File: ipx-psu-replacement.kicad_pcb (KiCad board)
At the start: 2 copper layers, 226 x 81 mm, 16 parts, among them J1 L, J10 -12V, J11 GND, J2 AC IN, J3 GND, J4 Floppy, J5 AC OUT, J6 N, J7 +12V, J8 +5V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

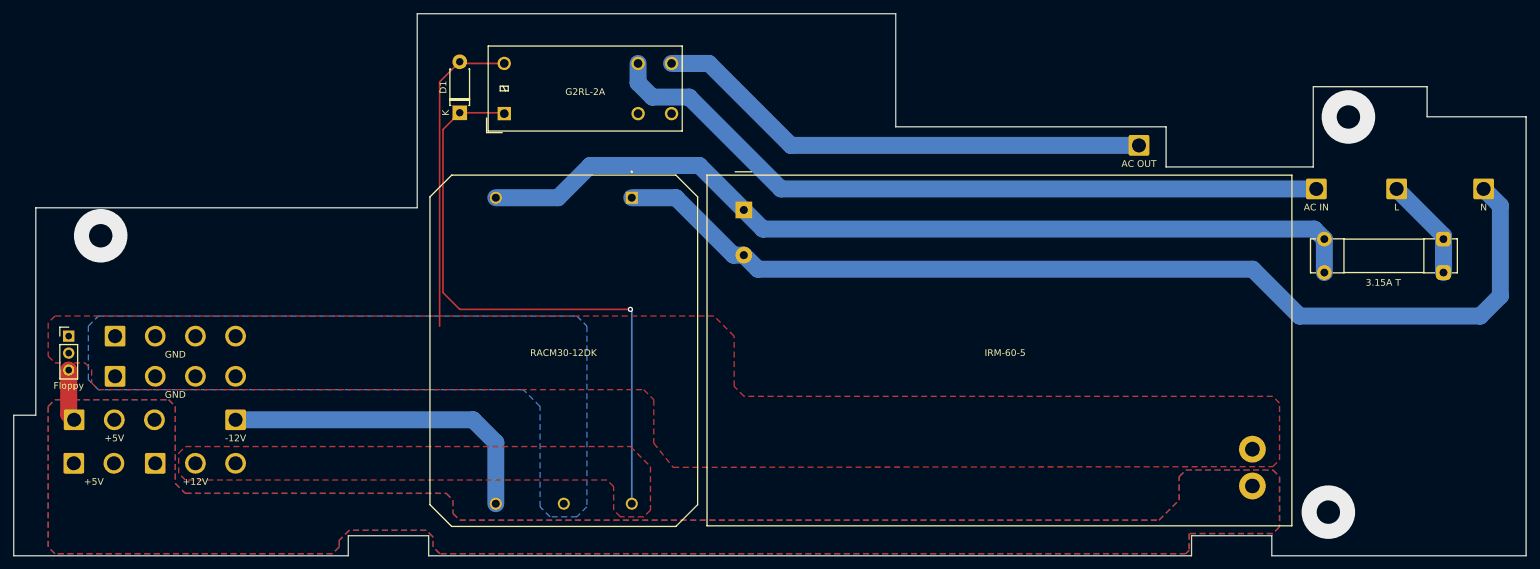
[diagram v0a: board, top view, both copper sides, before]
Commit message: add power good sensing
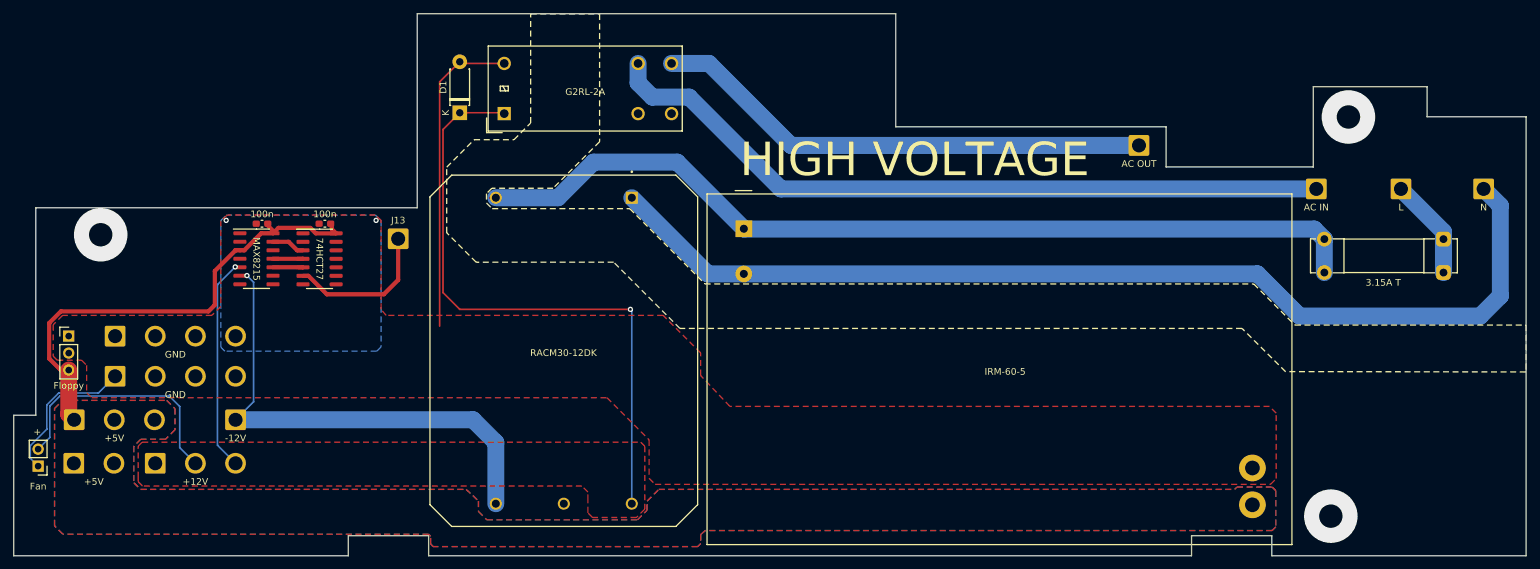
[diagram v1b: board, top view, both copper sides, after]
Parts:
- added C1: 100n, Capacitor_SMD:C_0603_1608Metric_Pad1.08x0.95mm_HandSolder, F.Cu at (76.5, 90.2)
- added C2: 100n, Capacitor_SMD:C_0603_1608Metric_Pad1.08x0.95mm_HandSolder, F.Cu at (85.8, 90.2)
- added J12: Fan, Connector_PinHeader_2.54mm:PinHeader_1x02_P2.54mm_Vertical, F.Cu at (43.0, 126.4)
- added J13: SENS, Connector_Wire:SolderWire-1.5sqmm_1x01_D1.7mm_OD3mm, F.Cu at (96.8, 92.5)
- added U1: 74HCT27, Package_SO:SO-14_3.9x8.65mm_P1.27mm, F.Cu at (85.0, 95.5)
- added U2: MAX8215, Package_SO:SO-14_3.9x8.65mm_P1.27mm, F.Cu at (75.6, 95.4)
- moved PS1 2.81 mm to (148.4, 91.0)
- moved J1 0.65 mm to (246.7, 85.0)
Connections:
- net /GND renamed GND
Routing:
- net /+12V: track 92.8 -> 162.4 mm, vias 1 -> 2
- net /+5V: track 7.77 -> 72.1 mm
- net /-12V: track 49.4 -> 73.6 mm, vias 0 -> 1
- net GND: track 47.5 -> 70.1 mm, vias 0 -> 2
- net Net-(J13-Pin_1): track 0.00 -> 22.4 mm
- net Net-(U2-OUT1): track 0.00 -> 5.01 mm
- net Net-(U2-OUT4): track 0.00 -> 4.48 mm
- net Net-(U2-OUT3): track 0.00 -> 4.48 mm
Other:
- board text added: "+"
- board text added: "HIGH VOLTAGE"

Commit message: supervisor circuitry fixed & improved
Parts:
- added C3: 1µ, Capacitor_SMD:C_0603_1608Metric_Pad1.08x0.95mm_HandSolder, F.Cu at (79.7, 104.5)
- added R1: 680k, Resistor_SMD:R_0603_1608Metric_Pad0.98x0.95mm_HandSolder, F.Cu at (72.1, 101.4)
- added R2: 680k, Resistor_SMD:R_0603_1608Metric_Pad0.98x0.95mm_HandSolder, F.Cu at (75.9, 101.4)
- added R3: 680k, Resistor_SMD:R_0603_1608Metric_Pad0.98x0.95mm_HandSolder, F.Cu at (79.7, 101.4)
- added R4: 680k, Resistor_SMD:R_0603_1608Metric_Pad0.98x0.95mm_HandSolder, F.Cu at (83.5, 101.4)
- D1: value 1N4001 -> PMEG2010ER; footprint Diode_THT:D_DO-41_SOD81_P7.62mm_Horizontal -> Diode_SMD:D_SOD-123
- moved D1 3.79 mm to (106.8, 69.9)
- moved C1 0.20 mm to (76.5, 90.0)
- moved C2 0.20 mm to (85.8, 90.0)
- moved J1 0.14 mm to (246.8, 85.0)
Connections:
- U1 pad 3: Net-(U2-OUT1) -> Net-(U2-OUT3)
- U1 pad 4: Net-(U2-OUT3) -> Net-(U2-OUT4)
- U1 pad 5: Net-(U2-OUT4) -> Net-(U2-DOUT)
- U2 pad 13: Net-(U2-OUT1) -> Net-(U2-DIN)
- U2 pad 7: unconnected-(U2-DIN-Pad7) -> Net-(U2-DIN)
- U2 pad 9: unconnected-(U2-DOUT-Pad9) -> Net-(U2-DOUT)
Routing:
- net Net-(U2-DIN): track 0.00 -> 19.4 mm
- net Net-(U2-DOUT): track 0.00 -> 16.4 mm
- net /+5V: track 72.1 -> 88.3 mm, vias 0 -> 4
- net Net-(U2-OUT4): track 4.48 -> 12.2 mm
- net Net-(U2-OUT3): track 4.48 -> 11.7 mm
- net Net-(U2-OUT1): track 5.01 -> 0.00 mm
- net /+12V: track 162.4 -> 166.2 mm
- net /-12V: track 73.6 -> 76.0 mm
- net Net-(PS1-AC/L): track 136.6 -> 135.8 mm
- net GND: track 70.1 -> 69.9 mm, vias 2 -> 8
- net (no net): vias 3 -> 0
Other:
- outline, holes or cut-outs redrawn
- board text added: "Sun APS-02 replacement PSU for SPARCstation IPX ©2023 Hans Hübner https://github.com/hanshuebner/ipx-psu-replacement"

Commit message: more adjustments
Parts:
- added J14: GND, Connector_Wire:SolderWire-2sqmm_1x01_D2mm_OD3.9mm, F.Cu at (52.2, 91.8)
- added J15: GND, Connector_Wire:SolderWire-2sqmm_1x01_D2mm_OD3.9mm, F.Cu at (235.3, 134.3)
- F1: footprint Fuse:Fuseholder_Clip-5x20mm_Bel_FC-203-22_Lateral_P17.80x5.00mm_D1.17mm_Horizontal -> Fuse:Fuseholder_Clip-5x20mm_Littelfuse_111_Inline_P20.00x5.00mm_D1.05mm_Horizontal
- K1: value G2RL-2A -> DH2U TV3
- moved F1 3.32 mm to (253.8, 94.3)
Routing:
- net Net-(PS1-AC/L): track 135.8 -> 135.1 mm
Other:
- outline, holes or cut-outs redrawn

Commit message: v1 - sent to production
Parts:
- moved J12 29.0 mm to (53.2, 99.3), turned to -90 degrees
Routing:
- net GND: track 69.9 -> 47.3 mm
- net /+12V: track 166.2 -> 169.5 mm
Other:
- board text added: "Sun APS-02 replacement PSU for SPARCstation IPX Version 1 - ©2023 Hans Hübner https://github.com/hanshuebner/ipx-psu-replacement"
- board text removed: "Sun APS-02 replacement PSU for SPARCstation IPX ©2023 Hans Hübner https://github.com/hanshuebner/ipx-psu-replacement"
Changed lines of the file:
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@@
   )
   (footprint "Connector_PinHeader_2.54mm:PinHeader_1x02_P2.54mm_Vertical" (layer "F.Cu")
-    (at 43 126.425 180)
+    (at 53.175 99.3 -90)
     (descr "Through hole straight pin header, 1x02, 2.54mm pitch, single row")
     (tags "Through hole pin header THT 1x02 2.54mm single row")
@@
     (property "ki_keywords" "connector")
     (attr through_hole)
-    (fp_text reference "J12" (at 0 -2.33) (layer "F.SilkS") hide
-        (effects (font (size 1 1) (thickness 0.15)))
-    )
-    (fp_text value "Fan" (at 0 -3.025 180) (layer "F.SilkS")
-        (effects (font (size 1 1) (thickness 0.15)))
-    )
-    (fp_text user "${REFERENCE}" (at 0 1.27 90) (layer "F.Fab")
+    (fp_text reference "J12" (at 0 -2.33 -270) (layer "F.SilkS") hide
+        (effects (font (size 1 1) (thickness 0.15)))
+    )
+    (fp_text value "Fan" (at 0 -3.025 -180) (layer "F.SilkS")
+        (effects (font (size 1 1) (thickness 0.15)))
+    )
+    (fp_text user "${REFERENCE}" (at 0 1.27) (layer "F.Fab")
         (effects (font (size 1 1) (thickness 0.15)))
     )
@@
     (fp_line (start 1.27 3.81) (end -1.27 3.81)
       (stroke (width 0.1) (type solid)) (layer "F.Fab"))
-    (pad "1" thru_hole rect (at 0 0 180) (size 1.7 1.7) (drill 1) (layers "*.Cu" "*.Mask")
+    (pad "1" thru_hole rect (at 0 0 270) (size 1.7 1.7) (drill 1) (layers "*.Cu" "*.Mask")
       (net 4 "GND") (pinfunction "Pin_1") (pintype "passive"))
-    (pad "2" thru_hole oval (at 0 2.54 180) (size 1.7 1.7) (drill 1) (layers "*.Cu" "*.Mask")
+    (pad "2" thru_hole oval (at 0 2.54 270) (size 1.7 1.7) (drill 1) (layers "*.Cu" "*.Mask")
       (net 1 "/+12V") (pinfunction "Pin_2") (pintype "passive"))
     (model "${KICAD6_3DMODEL_DIR}/Connector_PinHeader_2.54mm.3dshapes/PinHeader_1x02_P2.54mm_Vertical.wrl"
@@
     (effects (font (size 5 5) (thickness 0.5)) (justify left bottom))
   )
-  (gr_text "Sun APS-02 replacement\nPSU for SPARCstation IPX\n©2023 Hans Hübner\nhttps://github.com/hanshuebner/ipx-psu-replacement" (at 41.75 138.25) (layer "F.SilkS")
+  (gr_text "Sun APS-02 replacement PSU for SPARCstation IPX\nVersion 1 - ©2023 Hans Hübner\nhttps://github.com/hanshuebner/ipx-psu-replacement" (at 41.75 138.25) (layer "F.SilkS")
     (effects (font (size 1 1) (thickness 0.15)) (justify left bottom))
   )
-  (gr_text "+" (at 42.3 121.9) (layer "F.SilkS")
+  (gr_text "+" (at 47.6 99.8) (layer "F.SilkS")
     (effects (font (size 1 1) (thickness 0.15)) (justify left bottom))
   )
@@
   (via (at 72.45 96.65) (size 0.8) (drill 0.4) (layers "F.Cu" "B.Cu") (net 1))
   (via (at 131.5 103) (size 0.8) (drill 0.4) (layers "F.Cu" "B.Cu") (net 1))
-  (segment (start 64.15 123.65) (end 66.5 126) (width 0.25) (layer "B.Cu") (net 1))
   (segment (start 131.71 132.0375) (end 131.71 103.21) (width 0.25) (layer "B.Cu") (net 1))
-  (segment (start 43 123.885) (end 44.75 122.135) (width 0.25) (layer "B.Cu") (net 1))
+  (segment (start 63.1 101.4) (end 64.1 102.4) (width 0.635) (layer "B.Cu") (net 1))
   (segment (start 72.45 96.65) (end 69.8 99.3) (width 0.25) (layer "B.Cu") (net 1))
   (segment (start 69.8 99.3) (end 69.8 123.3) (width 0.25) (layer "B.Cu") (net 1))
+  (segment (start 64.1 122.4) (end 60.5 126) (width 0.635) (layer "B.Cu") (net 1))
   (segment (start 131.71 103.21) (end 131.5 103) (width 0.25) (layer "B.Cu") (net 1))
-  (segment (start 62.6 115.95) (end 64.15 117.5) (width 0.25) (layer "B.Cu") (net 1))
-  (segment (start 46.25 115.95) (end 62.6 115.95) (width 0.25) (layer "B.Cu") (net 1))
-  (segment (start 44.75 117.45) (end 46.25 115.95) (width 0.25) (layer "B.Cu") (net 1))
-  (segment (start 44.75 122.135) (end 44.75 117.45) (width 0.25) (layer "B.Cu") (net 1))
+  (segment (start 50.635 100.435) (end 51.6 101.4) (width 0.635) (layer "B.Cu") (net 1))
+  (segment (start 64.1 102.4) (end 64.1 122.4) (width 0.635) (layer "B.Cu") (net 1))
   (segment (start 69.8 123.3) (end 72.5 126) (width 0.25) (layer "B.Cu") (net 1))
-  (segment (start 64.15 117.5) (end 64.15 123.65) (width 0.25) (layer "B.Cu") (net 1))
+  (segment (start 50.635 99.3) (end 50.635 100.435) (width 0.635) (layer "B.Cu") (net 1))
+  (segment (start 51.6 101.4) (end 63.1 101.4) (width 0.635) (layer "B.Cu") (net 1))
   (segment (start 234 85) (end 154 85) (width 2.54) (layer "B.Cu") (net 2))
   (segment (start 132.65 69.15) (end 132.65 66.25) (width 2.54) (layer "B.Cu") (net 2))
@@
   (segment (start 134.78 71.28) (end 132.65 69.15) (width 2.54) (layer "B.Cu") (net 2))
   (segment (start 154 85) (end 140.28 71.28) (width 2.54) (layer "B.Cu") (net 2))
-  (segment (start 246.65 85.05) (end 246.65 85) (width 2.54) (layer "B.Cu") (net 3))
   (segment (start 246.79 92.31) (end 248.75 94.27) (width 2.54) (layer "B.Cu") (net 3))
   (segment (start 246.79 85.01) (end 246.79 92.31) (width 2.54) (layer "B.Cu") (net 3))
@@
   (via (at 77.86 100.28) (size 0.8) (drill 0.4) (layers "F.Cu" "B.Cu") (free) (net 4))
   (via (at 71.1 89.7) (size 0.8) (drill 0.4) (layers "F.Cu" "B.Cu") (free) (net 4))
-  (segment (start 52 115.5) (end 54.5 113) (width 0.25) (layer "B.Cu") (net 4))
-  (segment (start 43 126.425) (end 41.825 125.25) (width 0.25) (layer "B.Cu") (net 4))
-  (segment (start 46.063604 115.5) (end 52 115.5) (width 0.25) (layer "B.Cu") (net 4))
-  (segment (start 44.3 120.9) (end 44.3 117.263604) (width 0.25) (layer "B.Cu") (net 4))
-  (segment (start 44.3 117.263604) (end 46.063604 115.5) (width 0.25) (layer "B.Cu") (net 4))
-  (segment (start 41.825 123.375) (end 44.3 120.9) (width 0.25) (layer "B.Cu") (net 4))
-  (segment (start 41.825 125.25) (end 41.825 123.375) (width 0.25) (layer "B.Cu") (net 4))
   (segment (start 75.33 94.17) (end 73.15 94.17) (width 0.635) (layer "F.Cu") (net 5))
   (segment (start 46.4 103.3) (end 44.65 105.05) (width 0.635) (layer "F.Cu") (net 5))
@@
         (xy 241.75 139.25)
         (xy 242.5 138.5)
-        (xy 242.5 118.25)
-        (xy 241.75 117.5)
-        (xy 146.368411 117.5)
-        (xy 142 112.8889)
-        (xy 142 109.5)
-        (xy 136.4 103.9)
+        (xy 242.5 127.25)
+        (xy 232.75 117.5)
+        (xy 146.9 117.5)
+        (xy 133.7 103.9)
         (xy 95 103.9)
         (xy 94.25 103)
@@
         (xy 51 116.2)
         (xy 128 116.2)
-        (xy 134.3 122.5)
-        (xy 134.3 127.75)
-        (xy 134.878572 128.65)
+        (xy 141.2 128.65)
       )
     )
@@
         (xy 227.95 135.5)
         (xy 227.4 136.05)
-        (xy 142.7 136.05)
-        (xy 142 136.65)
-        (xy 142 138)
-        (xy 141.55 138.45)
-        (xy 102.014865 138.45)
-        (xy 101.65 138.05)
-        (xy 101.65 136.9)
+        (xy 145.4 136.05)
+        (xy 141.7 139.65)
+        (xy 104.2 139.65)
         (xy 101.35 136.6)
         (xy 46.7 136.6)
@@
         (xy 58.3 129.9)
         (xy 106.95 129.9)
-        (xy 107.968054 130.818054)
-        (xy 108.8 131.65)
-        (xy 108.8 133.2)
-        (xy 110.05 134.45)
-        (xy 132.55 134.45)
-        (xy 134 133)
-        (xy 134 131.65)
-        (xy 135.75 129.9)
+        (xy 111.5 134.45)
+        (xy 132.9 134.45)
+        (xy 137.3 129.9)
         (xy 221.8 129.9)
       )
@@
         (xy 224.65 99.2)
         (xy 230.8 105.35)
-        (xy 266.35 105.35)
-        (xy 266.35 110.4)
+        (xy 265.3 105.35)
         (xy 265.3 112.35)
         (xy 229.4 112.35)

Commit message: add base load resistors
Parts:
- added R5: 120, Resistor_THT:R_Axial_DIN0922_L20.0mm_D9.0mm_P25.40mm_Horizontal, F.Cu at (94.5, 133.4)
- added R6: 120, Resistor_THT:R_Axial_DIN0922_L20.0mm_D9.0mm_P25.40mm_Horizontal, F.Cu at (82.5, 133.4)
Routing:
- net /+12V: track 169.5 -> 186.0 mm
- net /-12V: track 76.0 -> 89.9 mm
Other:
- board text added: "Sun APS-02 replacement PSU for SPARCstation IPX Version 2 - ©2023 Hans Hübner https://github.com/hanshuebner/ipx-psu-replacement"
- board text removed: "Sun APS-02 replacement PSU for SPARCstation IPX Version 1 - ©2023 Hans Hübner https://github.com/hanshuebner/ipx-psu-replacement"

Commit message: hct27 -> hct11
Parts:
- U1: value 74HCT27 -> 74HCT11
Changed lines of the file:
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@@
         (effects (font (size 1 1) (thickness 0.15)))
     )
-    (fp_text value "74HCT27" (at 0 0 270 unlocked) (layer "F.SilkS")
+    (fp_text value "74HCT11" (at 0 0 270 unlocked) (layer "F.SilkS")
         (effects (font (size 1 1) (thickness 0.15)))
     )
